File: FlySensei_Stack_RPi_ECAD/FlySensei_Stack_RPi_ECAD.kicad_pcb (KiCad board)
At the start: 4 copper layers, 90 x 65 mm, 95 parts, among them J1 Conn_01x03, J10 Micro_SD_Card_Det, J2 USB_C_Receptacle_USB2.0, J3 Conn_02x20_Odd_Even_Male, J4 Conn_02x20_Odd_Even_Female, J5 Conn_02x20_Odd_Even_Male, J6 Conn_02x20_Odd_Even_Female, J7 Conn_01x22_Female, J8 Conn_01x22_Female, J9 Conn_01x14_Female, Q1 Q_NMOS_GSD, SW1 SW_SPST, SW2 SW_SPDT, SW3 SW_SPDT, U1 ComputeModule4-CM4, U10 RT9742GGJ5, U16 AP64501SP-13, U2 ATtiny85V-10S, U3 74LVC1G07, U4 G313-06329-00, U5 TPD2EUSB30, U6 TUSB321, U7 MPM3610, U8 TPD4EUSB30, U9 TPD4EUSB30

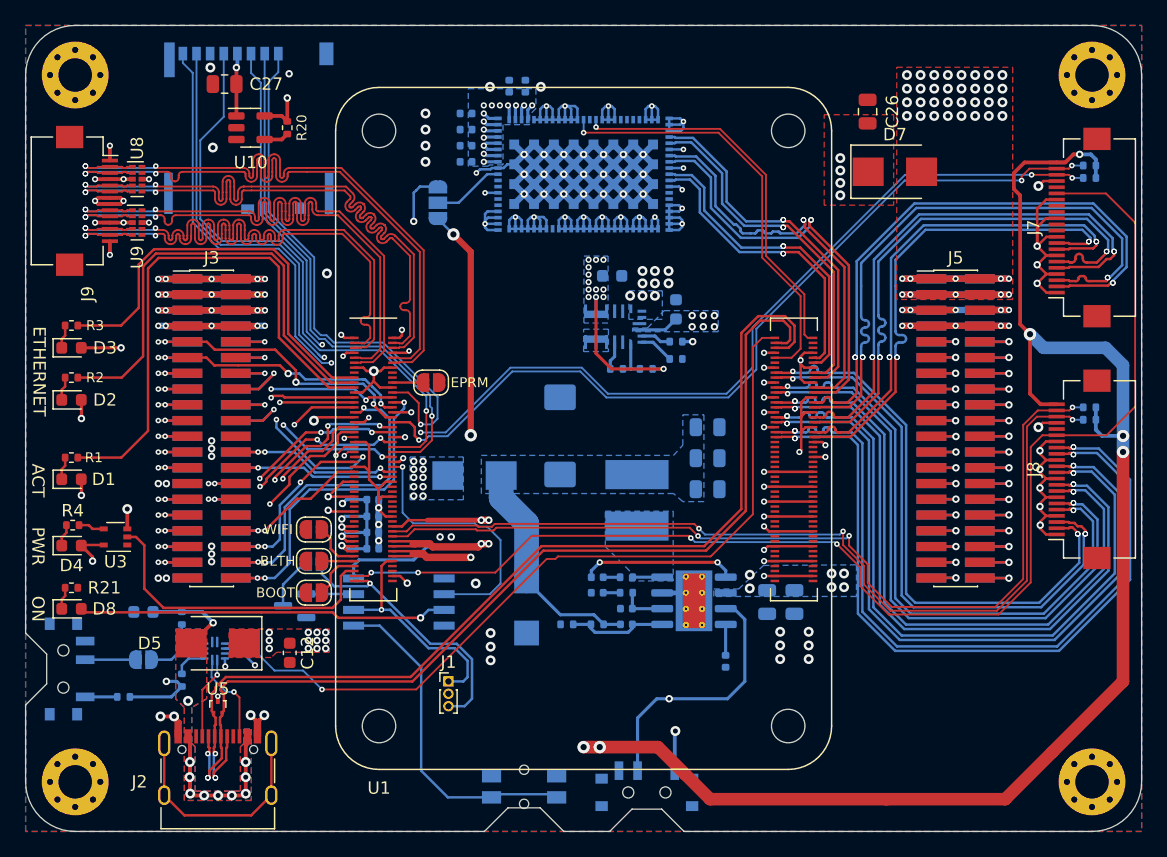
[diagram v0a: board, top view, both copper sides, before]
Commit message: Add PCB design for the actuation board
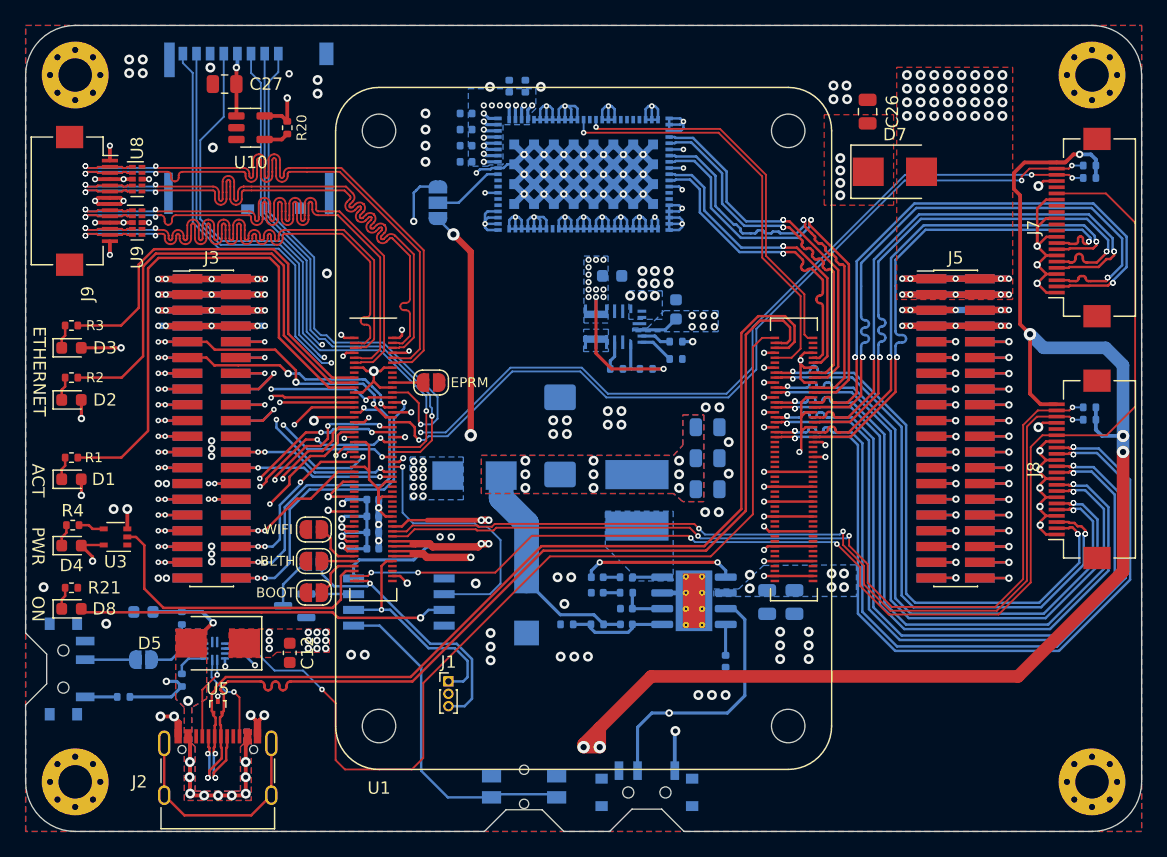
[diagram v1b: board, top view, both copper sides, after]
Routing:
- net /RPi_CM4/USB_ID: track 65.5 -> 77.1 mm
- net +3V3_RPI: track 165.7 -> 160.0 mm
- net /RPi_CM4/USB_DN: track 80.6 -> 82.3 mm
- net /PSU/PSU_EN: track 54.3 -> 55.7 mm
- net /AI/CORL_PCIE_TX_P: track 28.6 -> 29.6 mm
- net /AI/CORL_PCIE_CLK_P: track 24.2 -> 25.1 mm
- net /High Speed Interfaces/CAM0_MIPI.C_P: track 40.2 -> 41.0 mm
- net /AI/CORL_PCIE_RX_P: track 33.3 -> 33.8 mm
- net Net-(C18-Pad1): vias 0 -> 9
- net GND: vias 163 -> 201
- added copper zone on F.Cu, net Net-(C18-Pad1)
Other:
- outline, holes or cut-outs redrawn
